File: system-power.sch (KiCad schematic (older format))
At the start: 38 parts, among them J1 Conn_01x02, J2 Conn_01x02, U1 MCP73831T-2ACI/OT, U2 BQ25504, U5 TPS63031

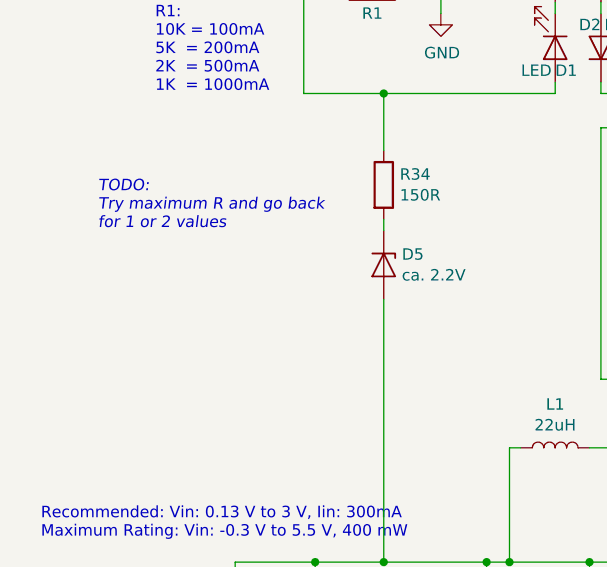
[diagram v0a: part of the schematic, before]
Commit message: Added footprint assignment
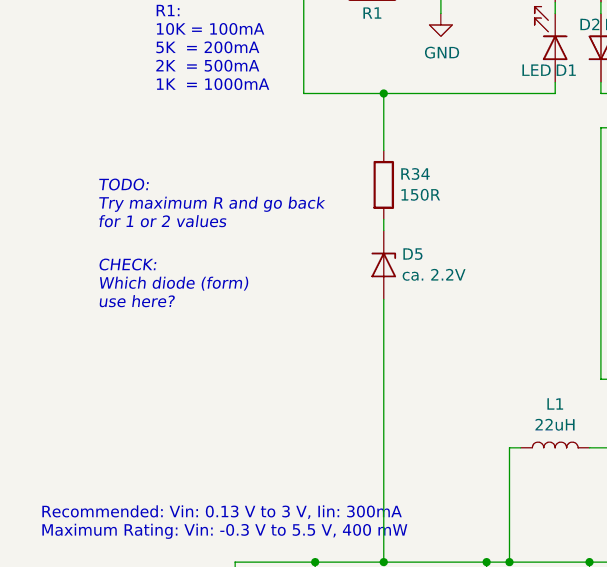
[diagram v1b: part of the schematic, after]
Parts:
- C50: footprint Capacitor_SMD:C_0402_1005Metric -> Capacitor_SMD:C_1206_3216Metric
- L1: footprint Inductor_SMD:L_0402_1005Metric -> Inductor_SMD:L_0805_2012Metric
- R34, R35, R36: footprint (none) -> Resistor_SMD:R_0402_1005Metric
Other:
- note added: "CHECK:\nWhich diode (form) \nuse here?"
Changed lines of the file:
@@
 F 0 "L1" V 3140 4250 50  0000 C CNN
 F 1 "22uH" V 3049 4250 50  0000 C CNN
-F 2 "Inductor_SMD:L_0402_1005Metric" H 2950 4250 50  0001 C CNN
+F 2 "Inductor_SMD:L_0805_2012Metric" H 2950 4250 50  0001 C CNN
 F 3 "~" H 2950 4250 50  0001 C CNN
 	1    2950 4250
@@
 F 0 "R34" H 2270 3146 50  0000 L CNN
 F 1 "150R" H 2270 3055 50  0000 L CNN
-F 2 "" V 2130 3100 50  0001 C CNN
+F 2 "Resistor_SMD:R_0402_1005Metric" V 2130 3100 50  0001 C CNN
 F 3 "~" H 2200 3100 50  0001 C CNN
 	1    2200 3100
@@
 F 0 "R36" H 6820 3446 50  0000 L CNN
 F 1 "5.49M" H 6820 3355 50  0000 L CNN
-F 2 "" V 6680 3400 50  0001 C CNN
+F 2 "Resistor_SMD:R_0402_1005Metric" V 6680 3400 50  0001 C CNN
 F 3 "~" H 6750 3400 50  0001 C CNN
 	1    6750 3400
@@
 F 0 "R35" H 6820 3046 50  0000 L CNN
 F 1 "5.49M" H 6820 2955 50  0000 L CNN
-F 2 "" V 6680 3000 50  0001 C CNN
+F 2 "Resistor_SMD:R_0402_1005Metric" V 6680 3000 50  0001 C CNN
 F 3 "~" H 6750 3000 50  0001 C CNN
 	1    6750 3000
@@
 F 0 "C50" H 3965 1396 50  0000 L CNN
 F 1 "150uF" H 3965 1305 50  0000 L CNN
-F 2 "Capacitor_SMD:C_0402_1005Metric" H 3888 1200 50  0001 C CNN
+F 2 "Capacitor_SMD:C_1206_3216Metric" H 3888 1200 50  0001 C CNN
 F 3 "~" H 3850 1350 50  0001 C CNN
 	1    3850 1350
@@
 Wire Wire Line
 	1900 4750 2200 4750
+Text Notes 950  3650 0    50   Italic 0
+CHECK:\nWhich diode (form) \nuse here?
 $EndSCHEMATC

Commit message: Review done
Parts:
- removed R35, R36: 5.49M, Resistor_SMD:R_0402_1005Metric, symbol Device:R
- R7: value 4.42M -> 4.64M
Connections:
- net GND: now also U5.7 (PS/SYNC)
- net at R11.2, R8.2, U2.14 (VBAT): now also C6.1, U5.5 (Vin)
- net at C4.1, C5.1, U2.15 (VSTOR): no longer C6.1, U5.5 (Vin)
- net at C7.1, U5.8 (VinA): no longer U5.7 (PS/SYNC)
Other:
- note added: "Settings for BQ25504:\n\nVBAT_OV: 4.093 V\nVBAT_UV: 2.803 V\nVBAT_OK: 2.998 V\nVBAT_OK_HYST: 3.096 V\nVREF_SAMP: 0.8 V"
- note removed: "1.8 V - 5.5 V"
- note removed: "CAUTION:\nFootprint 1206"
- note removed: "CHECK:\nCheck these values!"
- note removed: "CHECK:\nIs a diode required \nhere?"
- note removed: "CHECK:\nVoltage divider for measurement\nthe battery voltage. \nAre R's correct?"
- note removed: "CHECK:\nWhich diode (form) \nuse here?"
- note removed: "Settings for BQ25504:\n\nVBAT_OV: 4.204 V\nVBAT_UV: 2.803 V\nVBAT_OK: 2.998 V\nVBAT_OK_HYST: 3.096 V\nVREF_SAMP: 0.8 V"
- note removed: "TODO:\nA high current consumption of the\ntransceiver let the voltage collapse.\nMeasure with KO before BQ, after BQ\nand after the DCDC-Converter to analyze \nwhere voltage collapses. Afterwards place\na corresponding C."
- moved on the sheet: C1, C3, C4, C49, C5, C6, C7, L1, R10, R12, R13, R15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

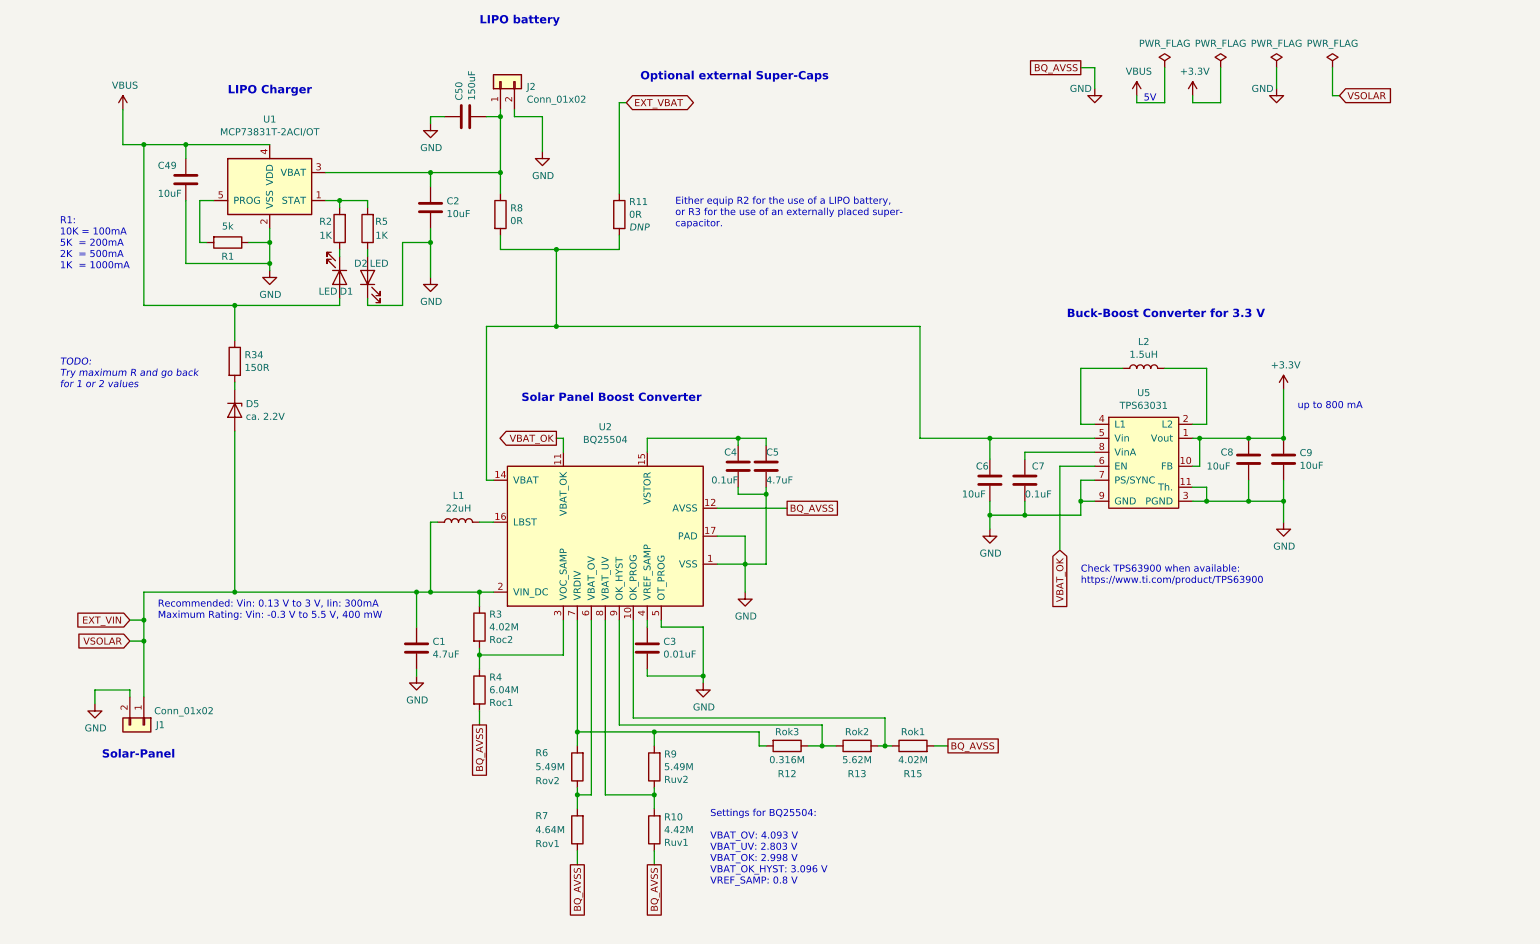
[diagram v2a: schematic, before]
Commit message: Major change of the layout (reviewed) for V1.1
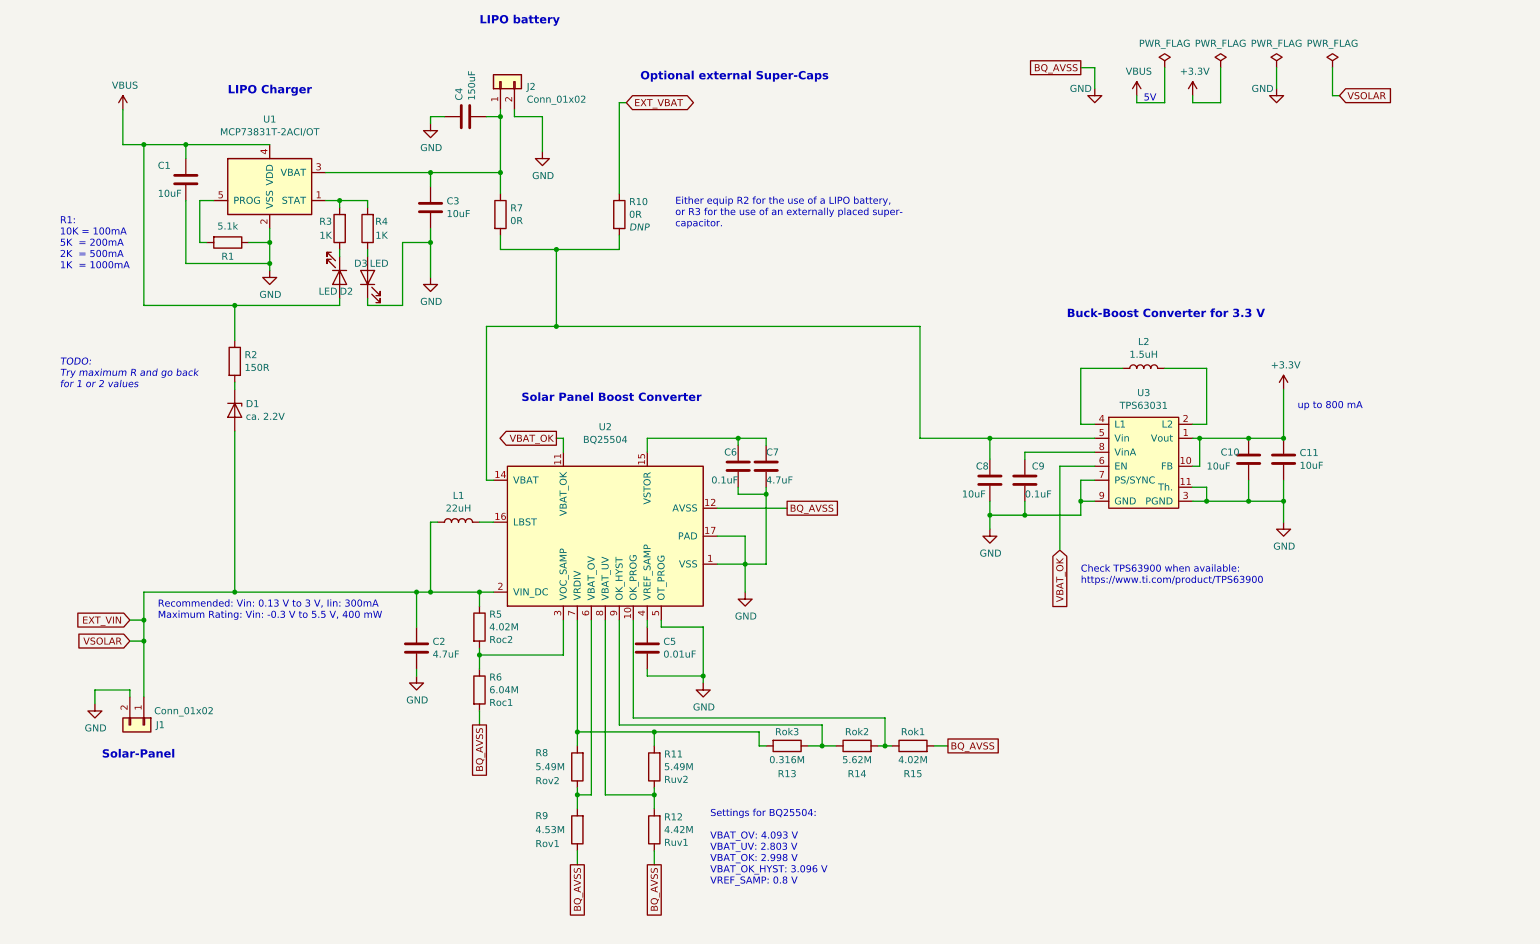
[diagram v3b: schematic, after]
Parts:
- D1: renamed from D5; footprint (none) -> Diode_SMD:D_SOD-323
- R1: value 5k -> 5.1k
- R9: renamed from R7; value 4.64M -> 4.53M
- renumbered C49 to C1, C8 to C10, C9 to C11, C1 to C2, C2 to C3, C50 to C4, C3 to C5, C4 to C6, C5 to C7, C6 to C8, C7 to C9, D1 to D2, D2 to D3, R11 to R10, R9 to R11, R10 to R12, R12 to R13, R13 to R14, R34 to R2, R2 to R3, R5 to R4, R3 to R5, R4 to R6, R8 to R7, R6 to R8, U5 to U3
